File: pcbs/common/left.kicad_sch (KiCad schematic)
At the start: 88 parts

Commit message: upload of pcb
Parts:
- removed C? (x2): 27p, Capacitor_SMD:C_0402_1005Metric, symbol Device:C_Small
- removed C? (x9): 100n, Capacitor_SMD:C_0402_1005Metric, symbol Device:C_Small
- removed C? (x3): 1u, Capacitor_SMD:C_0402_1005Metric, symbol Device:C_Small
- removed C? (x2): 10u, Capacitor_SMD:C_0402_1005Metric, symbol Device:C_Small
- removed D?: 1N4148WT, Diode_SMD:D_SOD-523, symbol Diode:1N4148WT
- removed EXLED? (x2), LED? (x21): YS-SK6812MINI-E, kbd_local:YS-SK6812MINI-E, symbol kbd_local:YS-SK6812MINI-E
- removed EXSW? (x2): RotaryEncoder_Switch, kbd_local:keyswitch_cherrymx_hotswap_1u_rotary_encoder_ec12, symbol Device:RotaryEncoder_Switch
- removed F?: BSMD0603-050-12V, Fuse:Fuse_0603_1608Metric, symbol Device:Fuse
- removed J?: TYPE-C-31-M-13C, kbd_local:TYPE-C-31-M-13C, symbol Connector:USB_C_Receptacle_USB2.0
- removed J?: Conn_01x03, Connector_PinHeader_2.54mm:PinHeader_1x03_P2.54mm_Vertical, symbol Connector_Generic:Conn_01x03
- removed JP1: SolderJumper_2_Bridged, Jumper:SolderJumper-2_P1.3mm_Open_RoundedPad1.0x1.5mm, symbol Jumper:SolderJumper_2_Bridged
- removed R? (x2): 27, Resistor_SMD:R_0402_1005Metric, symbol Device:R_Small
- removed R? (x2): 5.1k, Resistor_SMD:R_0402_1005Metric, symbol Device:R_Small
- removed R?: 10k, Resistor_SMD:R_0402_1005Metric, symbol Device:R
- removed R? (x2): 1k, Resistor_SMD:R_0402_1005Metric, symbol Device:R
- removed SMDSW? (x2): TS-1088R-02026, kbd_local:TS-1088R-02026, symbol Switch:SW_Push
- removed U?: RP2040, Package_DFN_QFN:QFN-56-1EP_7x7mm_P0.4mm_EP3.2x3.2mm, symbol MCU_RaspberryPi:RP2040
- removed U?: TPD4E05U06DQAR, Package_SON:USON-10_2.5x1.0mm_P0.5mm, symbol Power_Protection:TPD4EUSB30
- removed U?: W25Q128JVSIQ, Package_SO:SOIC-8_5.23x5.23mm_P1.27mm, symbol Memory_Flash:W25Q128JVS
- removed U?: NCP1117LPST33T3G, Package_TO_SOT_SMD:SOT-223-3_TabPin2, symbol Regulator_Linear:NCP1117-3.3_SOT223
- removed Y?: 12MHz 18pF, Crystal:Crystal_SMD_3225-4Pin_3.2x2.5mm, symbol Device:Crystal_GND24_Small
- removed ZD?: ESD5Z5V0C, Diode_SMD:D_SOD-523, symbol Diode:ESD5Zxx
- added D3, D4: WS2812B, LED_SMD:LED_WS2812B_PLCC4_5.0x5.0mm_P3.2mm, symbol LED:WS2812B
- added LED22, LED24, LED25, LED27, LED28, LED30, LED31, LED33, LED34, LED36, LED37, LED39, LED40, LED41, LED42: MX_SK6812MINI-E, PCM_marbastlib-mx:LED_MX_6028R-ROT, symbol PCM_marbastlib-mx:MX_SK6812MINI-E
- added LED23, LED26, LED29, LED32, LED35, LED38: MX_SK6812MINI-E, PCM_marbastlib-mx:LED_MX_6028R, symbol PCM_marbastlib-mx:MX_SK6812MINI-E
- added U5: rp2040, various:rp2040promicro, symbol PCM_marbastlib-promicroish:rp2040
- SW1: renamed from SW?; footprint kbd:keyswitch_cherrymx_hotswap_1.5u -> PCM_marbastlib-mx:SW_MX_HS_CPG151101S11_1u
- SW10, SW11, SW12, SW13, SW14, SW15, SW16, SW17, SW18, SW19, SW2, SW20, SW21, SW3, SW4, SW5, SW6, SW7, SW8, SW9: renamed from SW?; footprint kbd:keyswitch_cherrymx_hotswap_1u -> PCM_marbastlib-mx:SW_MX_HS_CPG151101S11_1u
- gave numbers to parts that had none: 2
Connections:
- net +5V: now also D3.1 (VDD), D4.1 (VDD), LED22.1 (VDD), LED23.1 (VDD), LED24.1 (VDD), LED25.1 (VDD), LED26.1 (VDD), LED27.1 (VDD), LED28.1 (VDD), LED29.1 (VDD), LED30.1 (VDD), LED31.1 (VDD), LED32.1 (VDD), LED33.1 (VDD), LED34.1 (VDD), LED35.1 (VDD), LED36.1 (VDD), LED37.1 (VDD), LED38.1 (VDD), LED39.1 (VDD), LED40.1 (VDD), LED41.1 (VDD), LED42.1 (VDD), U5.5v
- net GND: now also D3.3 (VSS), D4.3 (VSS), LED22.4 (VSS), LED23.4 (VSS), LED24.4 (VSS), LED25.4 (VSS), LED26.4 (VSS), LED27.4 (VSS), LED28.4 (VSS), LED29.4 (VSS), LED30.4 (VSS), LED31.4 (VSS), LED32.4 (VSS), LED33.4 (VSS), LED34.4 (VSS), LED35.4 (VSS), LED36.4 (VSS), LED37.4 (VSS), LED38.4 (VSS), LED39.4 (VSS), LED40.4 (VSS), LED41.4 (VSS), LED42.4 (VSS), U5.G (GND)
- net KEY1: now also U5.11 (GP11)
- net KEY10: now also U5.22 (GP22)
- net KEY11: now also U5.14 (GP14)
- net KEY12: now also U5.3 (GP3)
- net KEY13: now also U5.2 (GP2)
- net KEY14: now also U5.9 (GP9)
- net KEY15: now also U5.20 (GP20)
- net KEY16: now also U5.23 (GP23)
- net KEY17: now also U5.8 (GP8)
- net KEY18: now also U5.1 (GP1)
- net KEY19: now also U5.0 (GP0)
- net KEY2: now also U5.27 (GP27)
- net KEY20: now also U5.25 (GP25)
- net KEY21: now also U5.21 (GP21)
- net KEY3: now also U5.16 (GP16)
- net KEY4: now also U5.5 (GP5)
- net KEY5: now also U5.4 (GP4)
- net KEY6: now also U5.15 (GP15)
- net KEY7: now also U5.26 (GP26)
- net KEY8: now also U5.29 (GP29)
- net KEY9: now also U5.28 (GP28)
- net LED: now also D3.4 (DIN), U5.10 (GP10)
- net RX: now also U5.13 (GP13)
- net TX: now also U5.12 (GP12)
- net RE1A renamed SDA
- net SDA: now also U5.6 (GP6)
- net REB renamed SCL
- net SCL: now also U5.7 (GP7)
- new net: LED33.2 (DOUT), LED36.3 (DIN)
- new net: LED30.2 (DOUT), LED33.3 (DIN)
- new net: LED40.2 (DOUT), LED41.3 (DIN)
- new net: LED39.2 (DOUT), LED40.3 (DIN)
- new net: D3.2 (DOUT), D4.4 (DIN)
- new net: LED23.2 (DOUT), LED24.3 (DIN)
- new net: LED23.3 (DIN), LED26.2 (DOUT)
- new net: LED34.2 (DOUT), LED37.3 (DIN)
- new net: LED31.2 (DOUT), LED34.3 (DIN)
- new net: LED36.2 (DOUT), LED39.3 (DIN)
- new net: LED37.2 (DOUT), LED38.3 (DIN)
- new net: LED29.3 (DIN), LED32.2 (DOUT)
- new net: LED32.3 (DIN), LED35.2 (DOUT)
- new net: LED22.2 (DOUT), LED25.3 (DIN)
- new net: D4.2 (DOUT), LED22.3 (DIN)
- new net: LED27.2 (DOUT), LED30.3 (DIN)
- new net: LED41.2 (DOUT), LED42.3 (DIN)
- new net: LED26.3 (DIN), LED29.2 (DOUT)
- new net: LED35.3 (DIN), LED38.2 (DOUT)
- new net: LED25.2 (DOUT), LED28.3 (DIN)
- new net: LED24.2 (DOUT), LED27.3 (DIN)
- new net: LED28.2 (DOUT), LED31.3 (DIN)
- no-connect marks 3 -> 4
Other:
- note removed: "DEBUG"
- note removed: "Flash memory"
- note removed: "LDO"
- note removed: "LEDs"
- note removed: "USB ESD"
- note removed: "VBUS ESD"
- note removed: "boot switch"
- note removed: "close to pin 44"
- note removed: "close to pin 45"

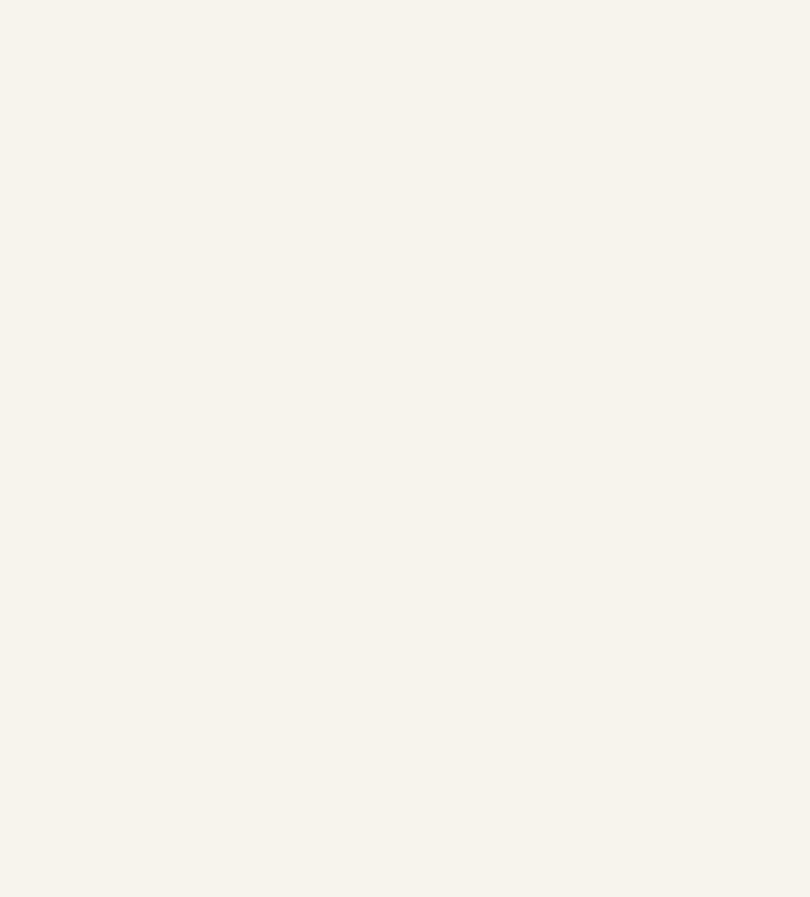
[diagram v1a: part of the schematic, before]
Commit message: split into left and right
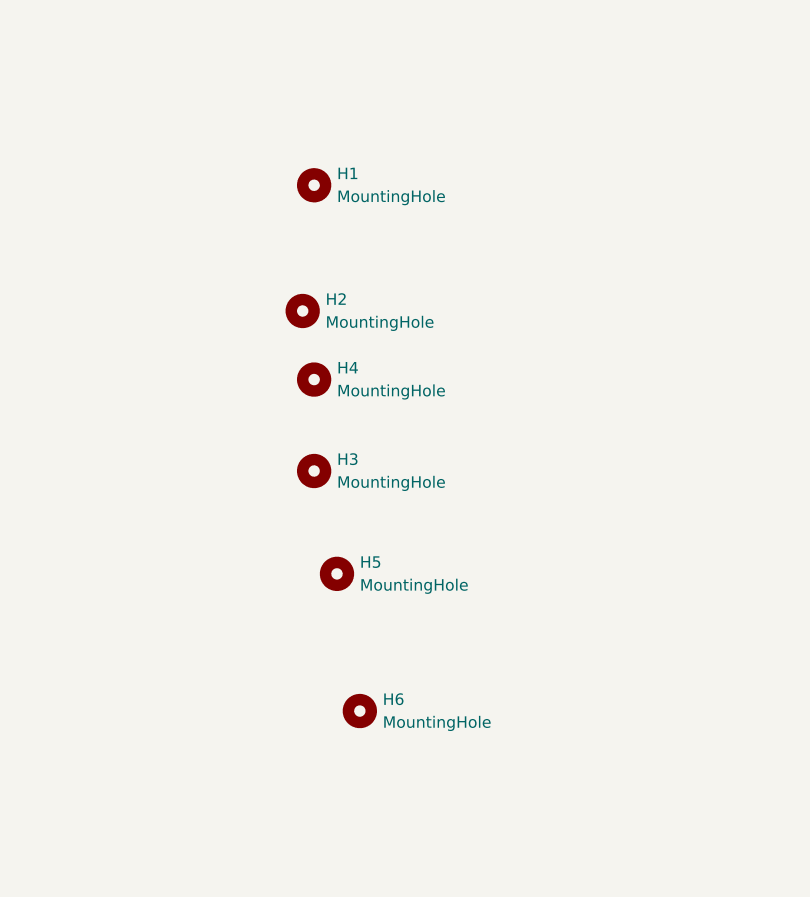
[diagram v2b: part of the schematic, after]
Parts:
- added H1, H2, H3, H4, H5, H6: MountingHole, MountingHole:MountingHole_2.2mm_M2, symbol Mechanical:MountingHole

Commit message: added zip files for prod
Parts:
- removed BT1, BT2, BT3, BT4: Breakaway Tabs, kbd_local:Breakaway_Tabs, symbol Mechanical:MountingHole
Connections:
- no-connect marks 4 -> 2
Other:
- note removed: "MCU RP2040"
- note removed: "SPLIT_HAND_PIN"
- moved on the sheet: D3, D4, LED22, LED23, LED24, LED25, LED26, LED27, LED28, LED29, LED30, LED31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
